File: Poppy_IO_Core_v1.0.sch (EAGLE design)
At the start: 97 parts, among them IC3 ATMEGA2560-16AU, IC6 LP2985-33DBVR, Q1 16MHz, Q2 16MHz, Q3 16MHz, Q4 16MHz, Q5 24MHz, U1 ATmega16u2, U2 MPU-6000, U3 USB2514B-AEZC, U4 ATmega16u2, U5 ATmega16u2, X1 1376408-SLOT_1.8V

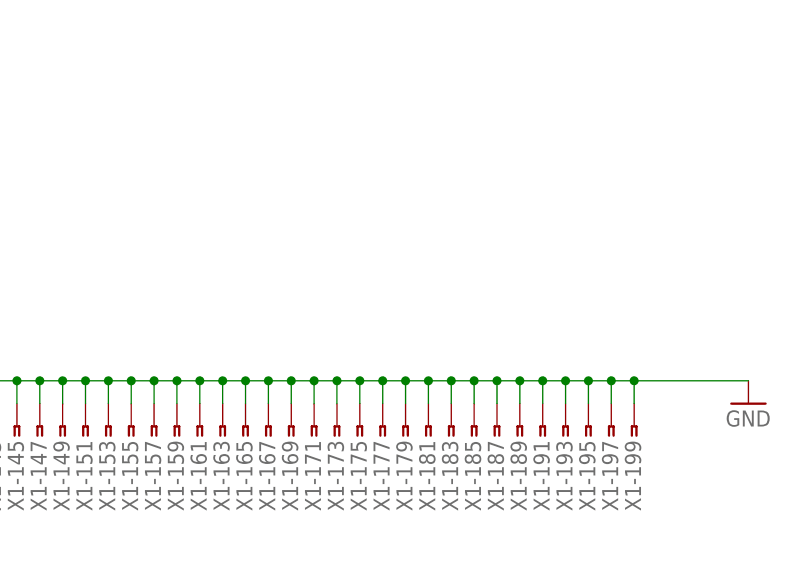
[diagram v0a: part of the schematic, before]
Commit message: Connected some (important) signals that had been omitted.
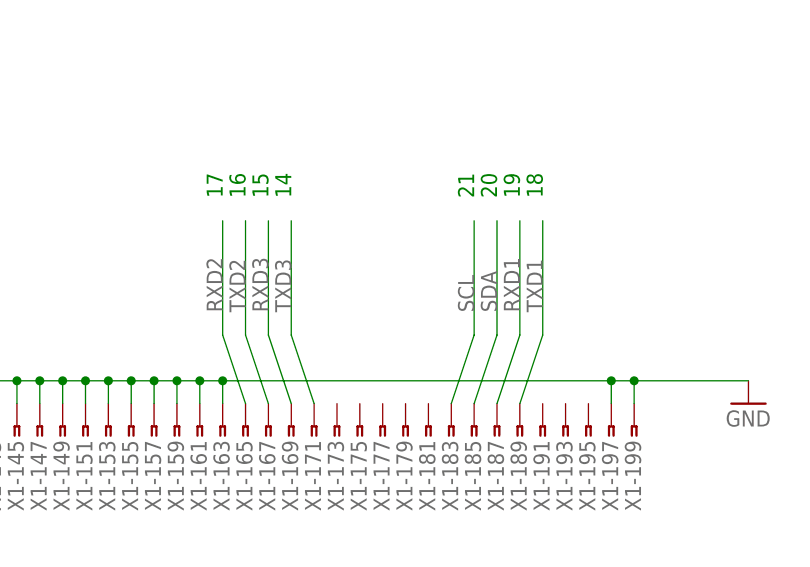
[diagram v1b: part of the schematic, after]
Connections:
- net GND: no longer X1-165.1, X1-167.1, X1-169.1, X1-171.1, X1-173.1, X1-175.1, X1-177.1, X1-179.1, X1-181.1, X1-183.1, X1-185.1, X1-187.1, X1-189.1, X1-191.1, X1-193.1, X1-195.1
- net RXD1: now also X1-187.1
- net RXD2: now also X1-165.1
- net RXD3: now also X1-169.1
- net SCL: now also X1-183.1
- net SDA: now also X1-185.1
- net TXD1: now also X1-189.1
- net TXD2: now also X1-167.1
- net TXD3: now also X1-171.1
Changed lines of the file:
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@@
 <?xml version="1.0" encoding="utf-8"?>
 <!DOCTYPE eagle SYSTEM "eagle.dtd">
-<eagle version="6.6.0">
+<eagle version="7.1.0">
 <drawing>
 <settings>
@@
 <text x="251.46" y="619.76" size="7.62" layer="97">Mega-compatible MCU</text>
 <text x="134.62" y="55.88" size="1.778" layer="91" rot="MR270">HWB</text>
+<text x="276.86" y="127" size="1.778" layer="91" rot="R90">15</text>
+<text x="274.32" y="127" size="1.778" layer="91" rot="R90">16</text>
+<text x="271.78" y="127" size="1.778" layer="91" rot="R90">17</text>
+<text x="307.34" y="127" size="1.778" layer="91" rot="R90">18</text>
+<text x="304.8" y="127" size="1.778" layer="91" rot="R90">19</text>
+<text x="302.26" y="127" size="1.778" layer="91" rot="R90">20</text>
+<text x="299.72" y="127" size="1.778" layer="91" rot="R90">21</text>
+<text x="279.4" y="127" size="1.778" layer="91" rot="R90">14</text>
 </plain>
 <instances>
@@
 <wire x1="266.7" y1="106.68" x2="269.24" y2="106.68" width="0.1524" layer="91"/>
 <wire x1="269.24" y1="106.68" x2="271.78" y2="106.68" width="0.1524" layer="91"/>
-<wire x1="271.78" y1="106.68" x2="274.32" y2="106.68" width="0.1524" layer="91"/>
-<wire x1="274.32" y1="106.68" x2="276.86" y2="106.68" width="0.1524" layer="91"/>
-<wire x1="276.86" y1="106.68" x2="279.4" y2="106.68" width="0.1524" layer="91"/>
-<wire x1="279.4" y1="106.68" x2="281.94" y2="106.68" width="0.1524" layer="91"/>
-<wire x1="281.94" y1="106.68" x2="284.48" y2="106.68" width="0.1524" layer="91"/>
-<wire x1="284.48" y1="106.68" x2="287.02" y2="106.68" width="0.1524" layer="91"/>
-<wire x1="287.02" y1="106.68" x2="289.56" y2="106.68" width="0.1524" layer="91"/>
-<wire x1="289.56" y1="106.68" x2="292.1" y2="106.68" width="0.1524" layer="91"/>
-<wire x1="292.1" y1="106.68" x2="294.64" y2="106.68" width="0.1524" layer="91"/>
-<wire x1="294.64" y1="106.68" x2="297.18" y2="106.68" width="0.1524" layer="91"/>
-<wire x1="297.18" y1="106.68" x2="299.72" y2="106.68" width="0.1524" layer="91"/>
-<wire x1="299.72" y1="106.68" x2="302.26" y2="106.68" width="0.1524" layer="91"/>
-<wire x1="302.26" y1="106.68" x2="304.8" y2="106.68" width="0.1524" layer="91"/>
-<wire x1="304.8" y1="106.68" x2="307.34" y2="106.68" width="0.1524" layer="91"/>
-<wire x1="307.34" y1="106.68" x2="309.88" y2="106.68" width="0.1524" layer="91"/>
-<wire x1="309.88" y1="106.68" x2="312.42" y2="106.68" width="0.1524" layer="91"/>
-<wire x1="312.42" y1="106.68" x2="314.96" y2="106.68" width="0.1524" layer="91"/>
+<wire x1="271.78" y1="106.68" x2="314.96" y2="106.68" width="0.1524" layer="91"/>
 <wire x1="314.96" y1="106.68" x2="317.5" y2="106.68" width="0.1524" layer="91"/>
 <wire x1="317.5" y1="106.68" x2="330.2" y2="106.68" width="0.1524" layer="91"/>
@@
 <pinref part="X1" gate="-163" pin="1"/>
 <wire x1="271.78" y1="106.68" x2="271.78" y2="104.14" width="0.1524" layer="91"/>
-<pinref part="X1" gate="-165" pin="1"/>
-<wire x1="274.32" y1="106.68" x2="274.32" y2="104.14" width="0.1524" layer="91"/>
-<pinref part="X1" gate="-167" pin="1"/>
-<wire x1="276.86" y1="106.68" x2="276.86" y2="104.14" width="0.1524" layer="91"/>
-<pinref part="X1" gate="-169" pin="1"/>
-<wire x1="279.4" y1="106.68" x2="279.4" y2="104.14" width="0.1524" layer="91"/>
-<pinref part="X1" gate="-171" pin="1"/>
-<wire x1="281.94" y1="106.68" x2="281.94" y2="104.14" width="0.1524" layer="91"/>
-<pinref part="X1" gate="-173" pin="1"/>
-<wire x1="284.48" y1="106.68" x2="284.48" y2="104.14" width="0.1524" layer="91"/>
-<pinref part="X1" gate="-175" pin="1"/>
-<wire x1="287.02" y1="106.68" x2="287.02" y2="104.14" width="0.1524" layer="91"/>
-<pinref part="X1" gate="-177" pin="1"/>
-<wire x1="289.56" y1="106.68" x2="289.56" y2="104.14" width="0.1524" layer="91"/>
-<pinref part="X1" gate="-179" pin="1"/>
-<wire x1="292.1" y1="106.68" x2="292.1" y2="104.14" width="0.1524" layer="91"/>
-<pinref part="X1" gate="-181" pin="1"/>
-<wire x1="294.64" y1="106.68" x2="294.64" y2="104.14" width="0.1524" layer="91"/>
-<pinref part="X1" gate="-183" pin="1"/>
-<wire x1="297.18" y1="106.68" x2="297.18" y2="104.14" width="0.1524" layer="91"/>
-<pinref part="X1" gate="-185" pin="1"/>
-<wire x1="299.72" y1="106.68" x2="299.72" y2="104.14" width="0.1524" layer="91"/>
-<pinref part="X1" gate="-187" pin="1"/>
-<wire x1="302.26" y1="106.68" x2="302.26" y2="104.14" width="0.1524" layer="91"/>
-<pinref part="X1" gate="-189" pin="1"/>
-<wire x1="304.8" y1="106.68" x2="304.8" y2="104.14" width="0.1524" layer="91"/>
-<pinref part="X1" gate="-191" pin="1"/>
-<wire x1="307.34" y1="106.68" x2="307.34" y2="104.14" width="0.1524" layer="91"/>
-<pinref part="X1" gate="-193" pin="1"/>
-<wire x1="309.88" y1="106.68" x2="309.88" y2="104.14" width="0.1524" layer="91"/>
-<pinref part="X1" gate="-195" pin="1"/>
-<wire x1="312.42" y1="106.68" x2="312.42" y2="104.14" width="0.1524" layer="91"/>
 <pinref part="X1" gate="-197" pin="1"/>
 <wire x1="314.96" y1="106.68" x2="314.96" y2="104.14" width="0.1524" layer="91"/>
 <junction x="314.96" y="106.68"/>
-<junction x="312.42" y="106.68"/>
-<junction x="309.88" y="106.68"/>
-<junction x="307.34" y="106.68"/>
-<junction x="304.8" y="106.68"/>
-<junction x="302.26" y="106.68"/>
-<junction x="299.72" y="106.68"/>
-<junction x="297.18" y="106.68"/>
-<junction x="294.64" y="106.68"/>
-<junction x="292.1" y="106.68"/>
-<junction x="289.56" y="106.68"/>
-<junction x="284.48" y="106.68"/>
-<junction x="287.02" y="106.68"/>
-<junction x="281.94" y="106.68"/>
-<junction x="279.4" y="106.68"/>
-<junction x="276.86" y="106.68"/>
-<junction x="274.32" y="106.68"/>
 <junction x="271.78" y="106.68"/>
 <junction x="269.24" y="106.68"/>
@@
 <pinref part="IC3" gate="1" pin="(SDA/INT1)PD1"/>
 </segment>
+<segment>
+<wire x1="302.26" y1="124.46" x2="302.26" y2="111.76" width="0.1524" layer="91"/>
+<label x="302.26" y="114.3" size="1.778" layer="95" rot="R90"/>
+<pinref part="X1" gate="-185" pin="1"/>
+<wire x1="302.26" y1="111.76" x2="299.72" y2="104.14" width="0.1524" layer="91"/>
+</segment>
 </net>
 <net name="SCL" class="0">
@@
 <pinref part="IC3" gate="1" pin="(SCL/INT0)PD0"/>
 </segment>
+<segment>
+<wire x1="299.72" y1="124.46" x2="299.72" y2="111.76" width="0.1524" layer="91"/>
+<label x="299.72" y="114.3" size="1.778" layer="95" rot="R90"/>
+<pinref part="X1" gate="-183" pin="1"/>
+<wire x1="299.72" y1="111.76" x2="297.18" y2="104.14" width="0.1524" layer="91"/>
+</segment>
 </net>
 <net name="ADC9" class="0">
@@
 <pinref part="IC3" gate="1" pin="(RXD1/INT2)PD2"/>
 </segment>
+<segment>
+<wire x1="304.8" y1="124.46" x2="304.8" y2="111.76" width="0.1524" layer="91"/>
+<label x="304.8" y="114.3" size="1.778" layer="95" rot="R90"/>
+<pinref part="X1" gate="-187" pin="1"/>
+<wire x1="304.8" y1="111.76" x2="302.26" y2="104.14" width="0.1524" layer="91"/>
+</segment>
 </net>
 <net name="TXD1" class="0">
@@
 <pinref part="IC3" gate="1" pin="(TXD1/INT3)PD3"/>
 </segment>
+<segment>
+<wire x1="307.34" y1="124.46" x2="307.34" y2="111.76" width="0.1524" layer="91"/>
+<label x="307.34" y="114.3" size="1.778" layer="95" rot="R90"/>
+<pinref part="X1" gate="-189" pin="1"/>
+<wire x1="307.34" y1="111.76" x2="304.8" y2="104.14" width="0.1524" layer="91"/>
+</segment>
 </net>
 <net name="RXD2" class="0">
@@
 <pinref part="IC3" gate="1" pin="PH0(RXD2)"/>
 </segment>
+<segment>
+<wire x1="271.78" y1="111.76" x2="271.78" y2="124.46" width="0.1524" layer="91"/>
+<label x="271.78" y="114.3" size="1.778" layer="95" rot="R90"/>
+<pinref part="X1" gate="-165" pin="1"/>
+<wire x1="274.32" y1="104.14" x2="271.78" y2="111.76" width="0.1524" layer="91"/>
+</segment>
 </net>
 <net name="RXD3" class="0">
@@
 <pinref part="IC3" gate="1" pin="PJ0(RXD3/PCINT9)"/>
 </segment>
+<segment>
+<wire x1="276.86" y1="111.76" x2="276.86" y2="124.46" width="0.1524" layer="91"/>
+<label x="276.86" y="114.3" size="1.778" layer="95" rot="R90"/>
+<pinref part="X1" gate="-169" pin="1"/>
+<wire x1="276.86" y1="111.76" x2="279.4" y2="104.14" width="0.1524" layer="91"/>
+</segment>
 </net>
 <net name="TXD2" class="0">
@@
 <pinref part="IC3" gate="1" pin="PH1(TXD2)"/>
 </segment>
+<segment>
+<wire x1="274.32" y1="111.76" x2="274.32" y2="124.46" width="0.1524" layer="91"/>
+<label x="274.32" y="114.3" size="1.778" layer="95" rot="R90"/>
+<pinref part="X1" gate="-167" pin="1"/>
+<wire x1="274.32" y1="111.76" x2="276.86" y2="104.14" width="0.1524" layer="91"/>
+</segment>
 </net>
 <net name="TXD3" class="0">
@@
 <pinref part="IC3" gate="1" pin="PJ1(TXD3/PCINT10)"/>
 </segment>
+<segment>
+<wire x1="279.4" y1="124.46" x2="279.4" y2="111.76" width="0.1524" layer="91"/>
+<label x="279.4" y="114.3" size="1.778" layer="95" rot="R90"/>
+<pinref part="X1" gate="-171" pin="1"/>
+<wire x1="279.4" y1="111.76" x2="281.94" y2="104.14" width="0.1524" layer="91"/>
+</segment>
 </net>
 <net name="PC0" class="0">
@@
 </sheet>
 </sheets>
-<errors>
-</errors>
 </schematic>
 </drawing>

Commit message: Aesthetics of the board done (text / logos)
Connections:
- net GND: now also X1-173.1, X1-181.1, X1-191.1; no longer X1-103.1, X1-105.1, X1-107.1, X1-109.1, X1-111.1, X1-113.1, X1-115.1, X1-117.1, X1-119.1, X1-121.1, X1-123.1, X1-125.1, X1-127.1, X1-129.1, X1-131.1, X1-133.1, X1-135.1, X1-137.1, X1-139.1, X1-141.1, X1-143.1, X1-145.1, X1-147.1, X1-149.1, X1-151.1, X1-153.1, X1-155.1, X1-157.1, X1-159.1, X1-161.1, X1-197.1
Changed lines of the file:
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@@
 <?xml version="1.0" encoding="utf-8"?>
 <!DOCTYPE eagle SYSTEM "eagle.dtd">
-<eagle version="7.1.0">
+<eagle version="6.6.0">
 <drawing>
 <settings>
@@
 <wire x1="185.42" y1="106.68" x2="187.96" y2="106.68" width="0.1524" layer="91"/>
 <wire x1="187.96" y1="106.68" x2="193.04" y2="106.68" width="0.1524" layer="91"/>
-<wire x1="193.04" y1="106.68" x2="195.58" y2="106.68" width="0.1524" layer="91"/>
-<wire x1="195.58" y1="106.68" x2="198.12" y2="106.68" width="0.1524" layer="91"/>
-<wire x1="198.12" y1="106.68" x2="200.66" y2="106.68" width="0.1524" layer="91"/>
-<wire x1="200.66" y1="106.68" x2="203.2" y2="106.68" width="0.1524" layer="91"/>
-<wire x1="203.2" y1="106.68" x2="205.74" y2="106.68" width="0.1524" layer="91"/>
-<wire x1="205.74" y1="106.68" x2="208.28" y2="106.68" width="0.1524" layer="91"/>
-<wire x1="208.28" y1="106.68" x2="210.82" y2="106.68" width="0.1524" layer="91"/>
-<wire x1="210.82" y1="106.68" x2="213.36" y2="106.68" width="0.1524" layer="91"/>
-<wire x1="213.36" y1="106.68" x2="215.9" y2="106.68" width="0.1524" layer="91"/>
-<wire x1="215.9" y1="106.68" x2="218.44" y2="106.68" width="0.1524" layer="91"/>
-<wire x1="218.44" y1="106.68" x2="220.98" y2="106.68" width="0.1524" layer="91"/>
-<wire x1="220.98" y1="106.68" x2="223.52" y2="106.68" width="0.1524" layer="91"/>
-<wire x1="223.52" y1="106.68" x2="226.06" y2="106.68" width="0.1524" layer="91"/>
-<wire x1="226.06" y1="106.68" x2="228.6" y2="106.68" width="0.1524" layer="91"/>
-<wire x1="228.6" y1="106.68" x2="231.14" y2="106.68" width="0.1524" layer="91"/>
-<wire x1="231.14" y1="106.68" x2="233.68" y2="106.68" width="0.1524" layer="91"/>
-<wire x1="233.68" y1="106.68" x2="236.22" y2="106.68" width="0.1524" layer="91"/>
-<wire x1="236.22" y1="106.68" x2="238.76" y2="106.68" width="0.1524" layer="91"/>
-<wire x1="238.76" y1="106.68" x2="241.3" y2="106.68" width="0.1524" layer="91"/>
-<wire x1="241.3" y1="106.68" x2="243.84" y2="106.68" width="0.1524" layer="91"/>
-<wire x1="243.84" y1="106.68" x2="246.38" y2="106.68" width="0.1524" layer="91"/>
-<wire x1="246.38" y1="106.68" x2="248.92" y2="106.68" width="0.1524" layer="91"/>
-<wire x1="248.92" y1="106.68" x2="251.46" y2="106.68" width="0.1524" layer="91"/>
-<wire x1="251.46" y1="106.68" x2="254" y2="106.68" width="0.1524" layer="91"/>
-<wire x1="254" y1="106.68" x2="256.54" y2="106.68" width="0.1524" layer="91"/>
-<wire x1="256.54" y1="106.68" x2="259.08" y2="106.68" width="0.1524" layer="91"/>
-<wire x1="259.08" y1="106.68" x2="261.62" y2="106.68" width="0.1524" layer="91"/>
-<wire x1="261.62" y1="106.68" x2="264.16" y2="106.68" width="0.1524" layer="91"/>
-<wire x1="264.16" y1="106.68" x2="266.7" y2="106.68" width="0.1524" layer="91"/>
-<wire x1="266.7" y1="106.68" x2="269.24" y2="106.68" width="0.1524" layer="91"/>
-<wire x1="269.24" y1="106.68" x2="271.78" y2="106.68" width="0.1524" layer="91"/>
-<wire x1="271.78" y1="106.68" x2="314.96" y2="106.68" width="0.1524" layer="91"/>
-<wire x1="314.96" y1="106.68" x2="317.5" y2="106.68" width="0.1524" layer="91"/>
+<wire x1="193.04" y1="106.68" x2="271.78" y2="106.68" width="0.1524" layer="91"/>
+<wire x1="271.78" y1="106.68" x2="284.48" y2="106.68" width="0.1524" layer="91"/>
+<wire x1="284.48" y1="106.68" x2="294.64" y2="106.68" width="0.1524" layer="91"/>
+<wire x1="294.64" y1="106.68" x2="307.34" y2="106.68" width="0.1524" layer="91"/>
+<wire x1="307.34" y1="106.68" x2="317.5" y2="106.68" width="0.1524" layer="91"/>
 <wire x1="317.5" y1="106.68" x2="330.2" y2="106.68" width="0.1524" layer="91"/>
 <wire x1="317.5" y1="104.14" x2="317.5" y2="106.68" width="0.1524" layer="91"/>
@@
 <pinref part="X1" gate="-101" pin="1"/>
 <wire x1="193.04" y1="106.68" x2="193.04" y2="104.14" width="0.1524" layer="91"/>
-<pinref part="X1" gate="-103" pin="1"/>
-<wire x1="195.58" y1="106.68" x2="195.58" y2="104.14" width="0.1524" layer="91"/>
-<pinref part="X1" gate="-105" pin="1"/>
-<wire x1="198.12" y1="106.68" x2="198.12" y2="104.14" width="0.1524" layer="91"/>
-<pinref part="X1" gate="-107" pin="1"/>
-<wire x1="200.66" y1="106.68" x2="200.66" y2="104.14" width="0.1524" layer="91"/>
-<pinref part="X1" gate="-109" pin="1"/>
-<wire x1="203.2" y1="106.68" x2="203.2" y2="104.14" width="0.1524" layer="91"/>
-<pinref part="X1" gate="-111" pin="1"/>
-<wire x1="205.74" y1="106.68" x2="205.74" y2="104.14" width="0.1524" layer="91"/>
-<pinref part="X1" gate="-113" pin="1"/>
-<wire x1="208.28" y1="106.68" x2="208.28" y2="104.14" width="0.1524" layer="91"/>
-<pinref part="X1" gate="-115" pin="1"/>
-<wire x1="210.82" y1="106.68" x2="210.82" y2="104.14" width="0.1524" layer="91"/>
-<pinref part="X1" gate="-117" pin="1"/>
-<wire x1="213.36" y1="106.68" x2="213.36" y2="104.14" width="0.1524" layer="91"/>
-<pinref part="X1" gate="-119" pin="1"/>
-<wire x1="215.9" y1="106.68" x2="215.9" y2="104.14" width="0.1524" layer="91"/>
-<pinref part="X1" gate="-121" pin="1"/>
-<wire x1="218.44" y1="106.68" x2="218.44" y2="104.14" width="0.1524" layer="91"/>
-<pinref part="X1" gate="-123" pin="1"/>
-<wire x1="220.98" y1="106.68" x2="220.98" y2="104.14" width="0.1524" layer="91"/>
-<pinref part="X1" gate="-125" pin="1"/>
-<wire x1="223.52" y1="106.68" x2="223.52" y2="104.14" width="0.1524" layer="91"/>
-<pinref part="X1" gate="-127" pin="1"/>
-<wire x1="226.06" y1="106.68" x2="226.06" y2="104.14" width="0.1524" layer="91"/>
-<pinref part="X1" gate="-129" pin="1"/>
-<wire x1="228.6" y1="106.68" x2="228.6" y2="104.14" width="0.1524" layer="91"/>
-<pinref part="X1" gate="-131" pin="1"/>
-<wire x1="231.14" y1="106.68" x2="231.14" y2="104.14" width="0.1524" layer="91"/>
-<pinref part="X1" gate="-133" pin="1"/>
-<wire x1="233.68" y1="106.68" x2="233.68" y2="104.14" width="0.1524" layer="91"/>
-<pinref part="X1" gate="-135" pin="1"/>
-<wire x1="236.22" y1="106.68" x2="236.22" y2="104.14" width="0.1524" layer="91"/>
-<pinref part="X1" gate="-137" pin="1"/>
-<wire x1="238.76" y1="106.68" x2="238.76" y2="104.14" width="0.1524" layer="91"/>
-<pinref part="X1" gate="-139" pin="1"/>
-<wire x1="241.3" y1="106.68" x2="241.3" y2="104.14" width="0.1524" layer="91"/>
-<pinref part="X1" gate="-141" pin="1"/>
-<wire x1="243.84" y1="106.68" x2="243.84" y2="104.14" width="0.1524" layer="91"/>
-<pinref part="X1" gate="-143" pin="1"/>
-<wire x1="246.38" y1="106.68" x2="246.38" y2="104.14" width="0.1524" layer="91"/>
-<pinref part="X1" gate="-145" pin="1"/>
-<wire x1="248.92" y1="106.68" x2="248.92" y2="104.14" width="0.1524" layer="91"/>
-<pinref part="X1" gate="-147" pin="1"/>
-<wire x1="251.46" y1="106.68" x2="251.46" y2="104.14" width="0.1524" layer="91"/>
-<pinref part="X1" gate="-149" pin="1"/>
-<wire x1="254" y1="106.68" x2="254" y2="104.14" width="0.1524" layer="91"/>
-<pinref part="X1" gate="-151" pin="1"/>
-<wire x1="256.54" y1="106.68" x2="256.54" y2="104.14" width="0.1524" layer="91"/>
-<pinref part="X1" gate="-153" pin="1"/>
-<wire x1="259.08" y1="106.68" x2="259.08" y2="104.14" width="0.1524" layer="91"/>
-<pinref part="X1" gate="-155" pin="1"/>
-<wire x1="261.62" y1="106.68" x2="261.62" y2="104.14" width="0.1524" layer="91"/>
-<pinref part="X1" gate="-157" pin="1"/>
-<wire x1="264.16" y1="106.68" x2="264.16" y2="104.14" width="0.1524" layer="91"/>
-<pinref part="X1" gate="-159" pin="1"/>
-<wire x1="266.7" y1="106.68" x2="266.7" y2="104.14" width="0.1524" layer="91"/>
-<pinref part="X1" gate="-161" pin="1"/>
-<wire x1="269.24" y1="106.68" x2="269.24" y2="104.14" width="0.1524" layer="91"/>
 <pinref part="X1" gate="-163" pin="1"/>
 <wire x1="271.78" y1="106.68" x2="271.78" y2="104.14" width="0.1524" layer="91"/>
-<pinref part="X1" gate="-197" pin="1"/>
-<wire x1="314.96" y1="106.68" x2="314.96" y2="104.14" width="0.1524" layer="91"/>
-<junction x="314.96" y="106.68"/>
 <junction x="271.78" y="106.68"/>
-<junction x="269.24" y="106.68"/>
-<junction x="266.7" y="106.68"/>
-<junction x="264.16" y="106.68"/>
-<junction x="261.62" y="106.68"/>
-<junction x="259.08" y="106.68"/>
-<junction x="256.54" y="106.68"/>
-<junction x="254" y="106.68"/>
-<junction x="251.46" y="106.68"/>
-<junction x="248.92" y="106.68"/>
-<junction x="246.38" y="106.68"/>
-<junction x="243.84" y="106.68"/>
-<junction x="241.3" y="106.68"/>
-<junction x="236.22" y="106.68"/>
-<junction x="238.76" y="106.68"/>
-<junction x="233.68" y="106.68"/>
-<junction x="231.14" y="106.68"/>
-<junction x="228.6" y="106.68"/>
-<junction x="226.06" y="106.68"/>
-<junction x="223.52" y="106.68"/>
-<junction x="220.98" y="106.68"/>
-<junction x="218.44" y="106.68"/>
-<junction x="215.9" y="106.68"/>
-<junction x="210.82" y="106.68"/>
-<junction x="213.36" y="106.68"/>
-<junction x="208.28" y="106.68"/>
-<junction x="200.66" y="106.68"/>
-<junction x="198.12" y="106.68"/>
-<junction x="195.58" y="106.68"/>
 <junction x="193.04" y="106.68"/>
-<junction x="203.2" y="106.68"/>
-<junction x="205.74" y="106.68"/>
 <pinref part="X1" gate="-77" pin="1"/>
 <wire x1="162.56" y1="106.68" x2="162.56" y2="104.14" width="0.1524" layer="91"/>
 <junction x="162.56" y="106.68"/>
+<pinref part="X1" gate="-181" pin="1"/>
+<wire x1="294.64" y1="104.14" x2="294.64" y2="106.68" width="0.1524" layer="91"/>
+<pinref part="X1" gate="-191" pin="1"/>
+<wire x1="307.34" y1="104.14" x2="307.34" y2="106.68" width="0.1524" layer="91"/>
+<pinref part="X1" gate="-173" pin="1"/>
+<wire x1="284.48" y1="104.14" x2="284.48" y2="106.68" width="0.1524" layer="91"/>
+<junction x="284.48" y="106.68"/>
+<junction x="294.64" y="106.68"/>
+<junction x="307.34" y="106.68"/>
 </segment>
 <segment>
